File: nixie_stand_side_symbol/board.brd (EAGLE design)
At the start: 25 x 30 mm, 2 parts

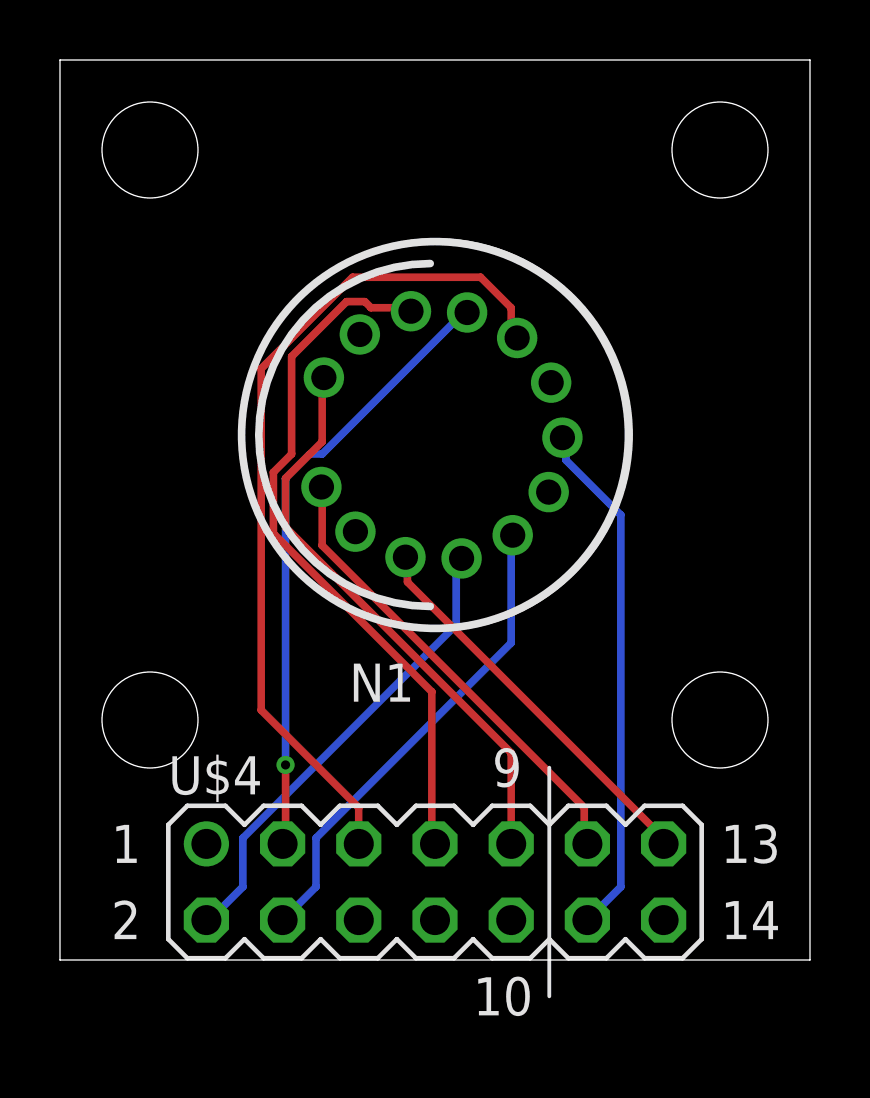
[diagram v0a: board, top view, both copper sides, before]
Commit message: [fix] 太さ・ガーバー出力(FusionPCB)
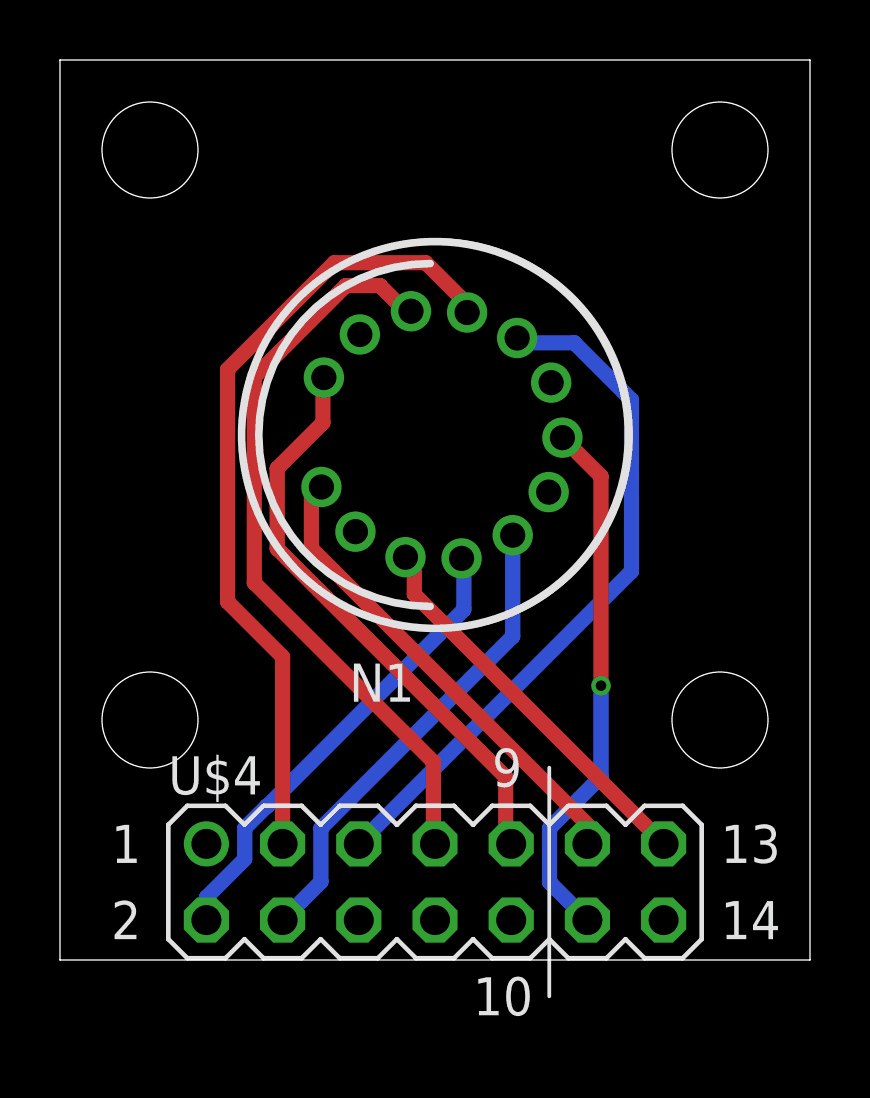
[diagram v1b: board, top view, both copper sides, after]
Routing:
- net NIXIE1: track 20.5 -> 26.9 mm, vias 1 -> 0
- net NIXIE2: track 28.3 -> 23.3 mm
- net NIXIE3: track 23.6 -> 25.3 mm
- net NIXIE5: track 15.5 -> 16.2 mm
- net N$1: track 17.3 -> 17.8 mm, vias 0 -> 1
